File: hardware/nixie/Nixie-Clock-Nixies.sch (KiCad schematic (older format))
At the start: 21 parts, among them J1 Nixies-Connector

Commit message: Add screw terminals for I/O, Improve PCB layout
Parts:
- N1, N2, N3, N4, N5, N6: symbol nixies-us:IN-4 -> Nixie-Clock-Nixies-rescue:IN-4-nixies-us
- N10, N7, N8, N9: symbol nixies-us:IN-6 -> Nixie-Clock-Nixies-rescue:IN-6-nixies-us
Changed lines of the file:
@@
 $EndDescr
 $Comp
-L nixies-us:IN-4 N1
+L Nixie-Clock-Nixies-rescue:IN-4-nixies-us N1
 U 1 1 61C656EE
 P 1250 2800
@@
 $EndComp
 $Comp
-L nixies-us:IN-4 N2
+L Nixie-Clock-Nixies-rescue:IN-4-nixies-us N2
 U 1 1 61C66B88
 P 2850 2800
@@
 $EndComp
 $Comp
-L nixies-us:IN-6 N8
+L Nixie-Clock-Nixies-rescue:IN-6-nixies-us N8
 U 1 1 61C679B4
 P 3950 3100
@@
 $EndComp
 $Comp
-L nixies-us:IN-6 N7
+L Nixie-Clock-Nixies-rescue:IN-6-nixies-us N7
 U 1 1 61C6976E
 P 3950 2600
@@
 $EndComp
 $Comp
-L nixies-us:IN-4 N3
+L Nixie-Clock-Nixies-rescue:IN-4-nixies-us N3
 U 1 1 61C6CBC4
 P 5100 2800
@@
 $EndComp
 $Comp
-L nixies-us:IN-4 N4
+L Nixie-Clock-Nixies-rescue:IN-4-nixies-us N4
 U 1 1 61C6CBCA
 P 6700 2800
@@
 $EndComp
 $Comp
-L nixies-us:IN-6 N10
+L Nixie-Clock-Nixies-rescue:IN-6-nixies-us N10
 U 1 1 61C6CBD0
 P 7850 3100
@@
 $EndComp
 $Comp
-L nixies-us:IN-6 N9
+L Nixie-Clock-Nixies-rescue:IN-6-nixies-us N9
 U 1 1 61C6CBD6
 P 7850 2600
@@
 $EndComp
 $Comp
-L nixies-us:IN-4 N5
+L Nixie-Clock-Nixies-rescue:IN-4-nixies-us N5
 U 1 1 61C6E7AE
 P 9000 2800
@@
 $EndComp
 $Comp
-L nixies-us:IN-4 N6
+L Nixie-Clock-Nixies-rescue:IN-4-nixies-us N6
 U 1 1 61C6E7B4
 P 10600 2800

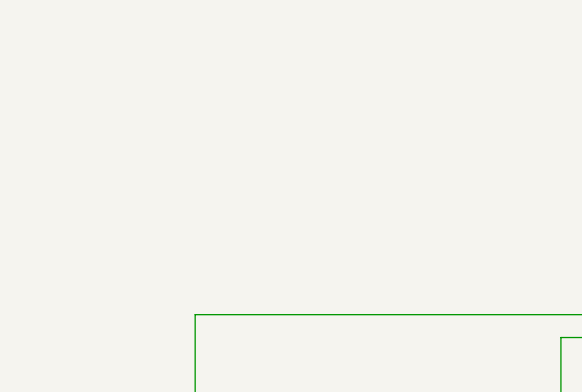
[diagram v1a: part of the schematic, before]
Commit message: Add Mounting Holes to PCB, Improve Routing, Add power pin header, Use correct connector footprint
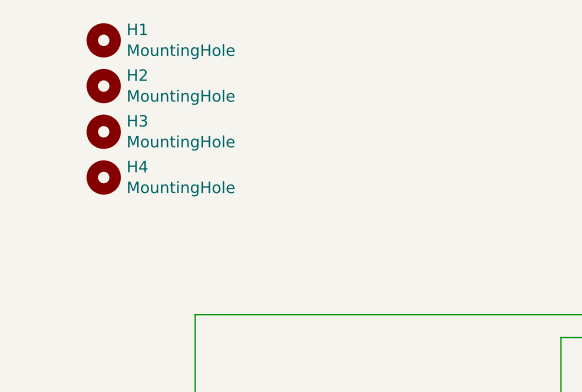
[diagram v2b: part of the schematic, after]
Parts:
- added H1, H2, H3, H4: MountingHole, MountingHole:MountingHole_2.7mm_M2.5, symbol Mechanical:MountingHole
- J1: footprint Connector_PinHeader_2.54mm:PinHeader_2x10_P2.54mm_Horizontal -> nixie-clock:PinHeader_2x10_P2.54mm_Horizontal_with_Interlock
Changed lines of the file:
@@
 F 0 "J1" V 5896 5612 50  0000 R CNN
 F 1 "Nixies-Connector" V 5805 5612 50  0000 R CNN
-F 2 "Connector_PinHeader_2.54mm:PinHeader_2x10_P2.54mm_Horizontal" H 5800 6200 50  0001 C CNN
+F 2 "nixie-clock:PinHeader_2x10_P2.54mm_Horizontal_with_Interlock" H 5800 6200 50  0001 C CNN
 F 3 "~" H 5800 6200 50  0001 C CNN
 	1    5800 6200
@@
 Wire Wire Line
 	3650 3450 3650 5100
+$Comp
+L Mechanical:MountingHole H2
+U 1 1 61CADA22
+P 850 1100
+F 0 "H2" H 950 1146 50  0000 L CNN
+F 1 "MountingHole" H 950 1055 50  0000 L CNN
+F 2 "MountingHole:MountingHole_2.7mm_M2.5" H 850 1100 50  0001 C CNN
+F 3 "~" H 850 1100 50  0001 C CNN
+	1    850  1100
+	1    0    0    -1
+$EndComp
+$Comp
+L Mechanical:MountingHole H3
+U 1 1 61CAE12D
+P 850 1300
+F 0 "H3" H 950 1346 50  0000 L CNN
+F 1 "MountingHole" H 950 1255 50  0000 L CNN
+F 2 "MountingHole:MountingHole_2.7mm_M2.5" H 850 1300 50  0001 C CNN
+F 3 "~" H 850 1300 50  0001 C CNN
+	1    850  1300
+	1    0    0    -1
+$EndComp
+$Comp
+L Mechanical:MountingHole H4
+U 1 1 61CAE6FB
+P 850 1500
+F 0 "H4" H 950 1546 50  0000 L CNN
+F 1 "MountingHole" H 950 1455 50  0000 L CNN
+F 2 "MountingHole:MountingHole_2.7mm_M2.5" H 850 1500 50  0001 C CNN
+F 3 "~" H 850 1500 50  0001 C CNN
+	1    850  1500
+	1    0    0    -1
+$EndComp
+$Comp
+L Mechanical:MountingHole H1
+U 1 1 61CACF00
+P 850 900
+F 0 "H1" H 950 946 50  0000 L CNN
+F 1 "MountingHole" H 950 855 50  0000 L CNN
+F 2 "MountingHole:MountingHole_2.7mm_M2.5" H 850 900 50  0001 C CNN
+F 3 "~" H 850 900 50  0001 C CNN
+	1    850  900
+	1    0    0    -1
+$EndComp
 $EndSCHEMATC

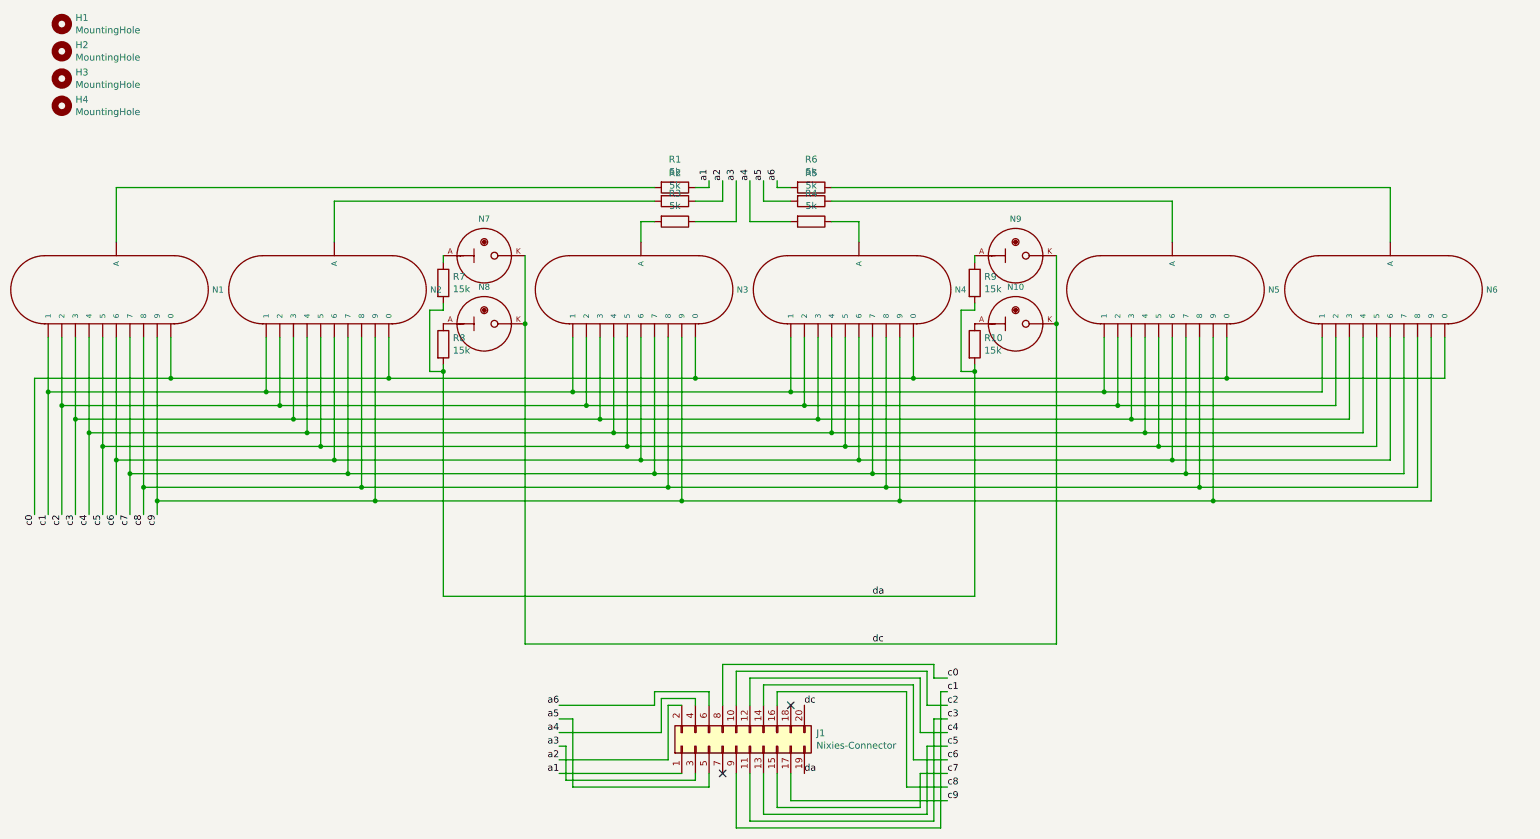
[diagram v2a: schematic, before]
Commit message: Fix libraries used in Nixie-Clock-Nixies
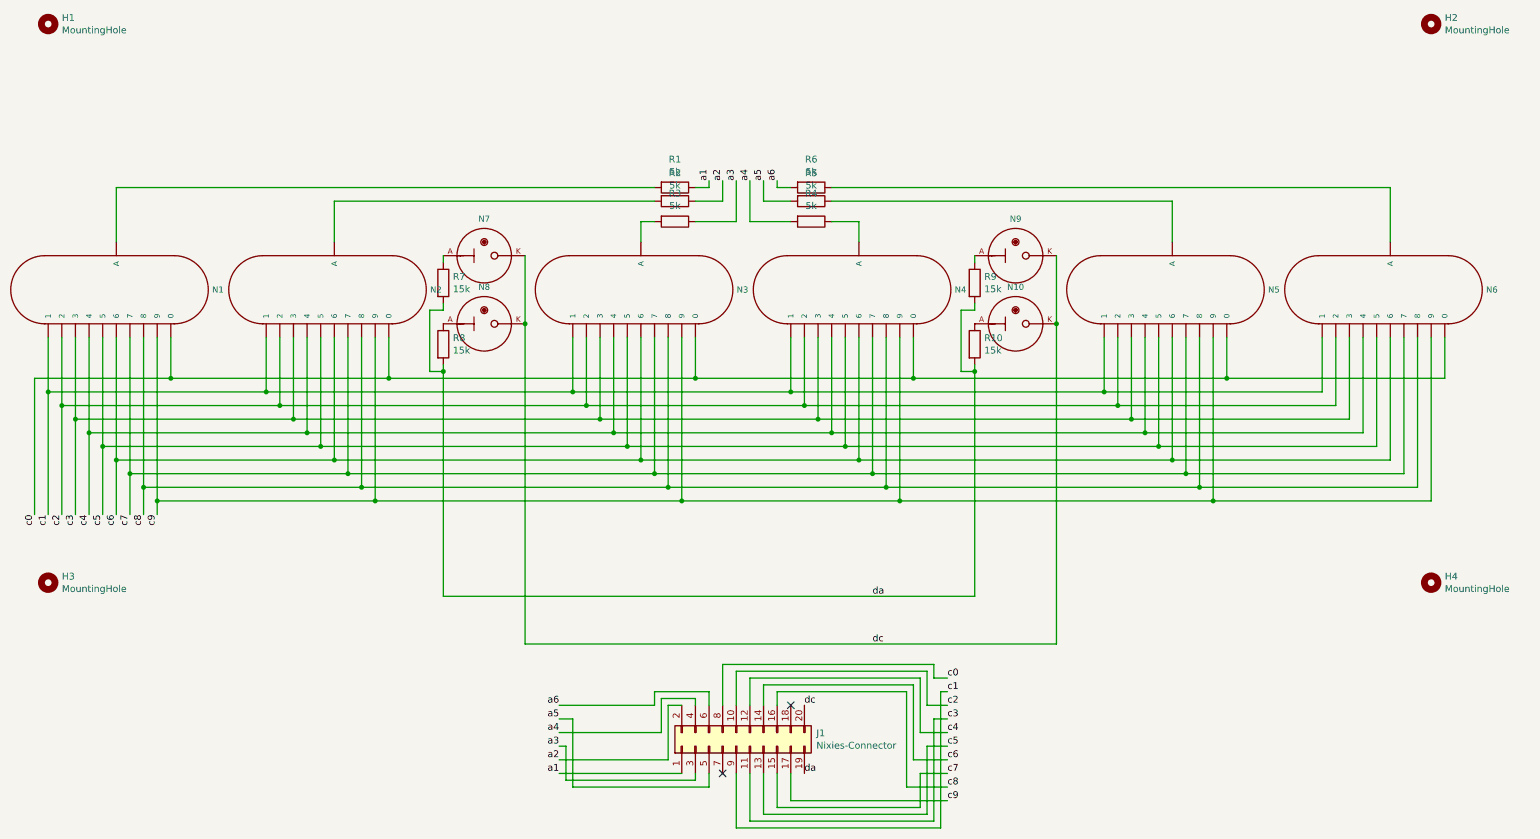
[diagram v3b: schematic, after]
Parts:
- removed N1, N2, N3, N4, N5, N6: IN-4, nixies-us:nixies-us-IN-4-DSUB, symbol Nixie-Clock-Nixies-rescue:IN-4-nixies-us
- removed N10, N7, N8, N9: IN-6, nixies-us:nixies-us-IN-6, symbol Nixie-Clock-Nixies-rescue:IN-6-nixies-us
- added N1, N2, N3, N4, N5, N6: IN-4, nixies-us:nixies-us-IN-4-DSUB, symbol nixies-us:IN-4
- added N10, N7, N8, N9: IN-6, nixies-us:nixies-us-IN-6, symbol nixies-us:IN-6
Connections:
- net c0: now also N1.0, N2.0, N3.0, N4.0, N5.0, N6.0
- net c1: now also N1.1, N2.1, N3.1, N4.1, N5.1, N6.1
- net c2: now also N1.2, N2.2, N3.2, N4.2, N5.2, N6.2
- net c3: now also N1.3, N2.3, N3.3, N4.3, N5.3, N6.3
- net c4: now also N1.4, N2.4, N3.4, N4.4, N5.4, N6.4
- net c5: now also N1.5, N2.5, N3.5, N4.5, N5.5, N6.5
- net c6: now also N1.6, N2.6, N3.6, N4.6, N5.6, N6.6
- net c7: now also N1.7, N2.7, N3.7, N4.7, N5.7, N6.7
- net c8: now also N1.8, N2.8, N3.8, N4.8, N5.8, N6.8
- net c9: now also N1.9, N2.9, N3.9, N4.9, N5.9, N6.9
- net dc: now also N10.K, N7.K, N8.K, N9.K
- net at R3.2: now also N3.A3 (A)
- net at R2.2: now also N2.A3 (A)
- net at R1.2: now also N1.A3 (A)
- net at R6.1: now also N6.A3 (A)
- net at R5.1: now also N5.A3 (A)
- net at R4.1: now also N4.A3 (A)
- net at R8.1: now also N8.A
- net at R7.1: now also N7.A
- net at R10.1: now also N10.A
- net at R9.1: now also N9.A
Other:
- moved on the sheet: H1, H2, H3, H4
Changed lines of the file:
@@
 encoding utf-8
 Sheet 1 1
-Title ""
-Date ""
-Rev ""
-Comp ""
+Title "Nixie-Clock: Nixies"
+Date "2021-12-25"
+Rev "1.0"
+Comp "Konrad Mösch"
 Comment1 ""
 Comment2 ""
@@
 Comment4 ""
 $EndDescr
-$Comp
-L Nixie-Clock-Nixies-rescue:IN-4-nixies-us N1
-U 1 1 61C656EE
-P 1250 2800
-F 0 "N1" V 1200 2097 45  0000 R CNN
-F 1 "IN-4" H 1250 2800 45  0001 L BNN
-F 2 "nixies-us:nixies-us-IN-4-DSUB" H 1280 2950 20  0001 C CNN
-F 3 "" H 1250 2800 50  0001 C CNN
-	1    1250 2800
-	0    -1   -1   0
-$EndComp
-$Comp
-L Nixie-Clock-Nixies-rescue:IN-4-nixies-us N2
-U 1 1 61C66B88
-P 2850 2800
-F 0 "N2" V 2800 2097 45  0000 R CNN
-F 1 "IN-4" H 2850 2800 45  0001 L BNN
-F 2 "nixies-us:nixies-us-IN-4-DSUB" H 2880 2950 20  0001 C CNN
-F 3 "" H 2850 2800 50  0001 C CNN
-	1    2850 2800
-	0    -1   -1   0
-$EndComp
-$Comp
-L Nixie-Clock-Nixies-rescue:IN-6-nixies-us N8
-U 1 1 61C679B4
-P 3950 3100
-F 0 "N8" H 3950 3370 45  0000 C CNN
-F 1 "IN-6" H 3950 3100 45  0001 L BNN
-F 2 "nixies-us:nixies-us-IN-6" H 3980 3250 20  0001 C CNN
-F 3 "" H 3950 3100 50  0001 C CNN
-	1    3950 3100
-	1    0    0    -1
-$EndComp
-$Comp
-L Nixie-Clock-Nixies-rescue:IN-6-nixies-us N7
-U 1 1 61C6976E
-P 3950 2600
-F 0 "N7" H 3950 2870 45  0000 C CNN
-F 1 "IN-6" H 3950 2600 45  0001 L BNN
-F 2 "nixies-us:nixies-us-IN-6" H 3980 2750 20  0001 C CNN
-F 3 "" H 3950 2600 50  0001 C CNN
-	1    3950 2600
-	1    0    0    -1
-$EndComp
-$Comp
-L Nixie-Clock-Nixies-rescue:IN-4-nixies-us N3
-U 1 1 61C6CBC4
-P 5100 2800
-F 0 "N3" V 5050 2097 45  0000 R CNN
-F 1 "IN-4" H 5100 2800 45  0001 L BNN
-F 2 "nixies-us:nixies-us-IN-4-DSUB" H 5130 2950 20  0001 C CNN
-F 3 "" H 5100 2800 50  0001 C CNN
-	1    5100 2800
-	0    -1   -1   0
-$EndComp
-$Comp
-L Nixie-Clock-Nixies-rescue:IN-4-nixies-us N4
-U 1 1 61C6CBCA
-P 6700 2800
-F 0 "N4" V 6650 2097 45  0000 R CNN
-F 1 "IN-4" H 6700 2800 45  0001 L BNN
-F 2 "nixies-us:nixies-us-IN-4-DSUB" H 6730 2950 20  0001 C CNN
-F 3 "" H 6700 2800 50  0001 C CNN
-	1    6700 2800
-	0    -1   -1   0
-$EndComp
-$Comp
-L Nixie-Clock-Nixies-rescue:IN-6-nixies-us N10
-U 1 1 61C6CBD0
-P 7850 3100
-F 0 "N10" H 7850 3370 45  0000 C CNN
-F 1 "IN-6" H 7850 3100 45  0001 L BNN
-F 2 "nixies-us:nixies-us-IN-6" H 7880 3250 20  0001 C CNN
-F 3 "" H 7850 3100 50  0001 C CNN
-	1    7850 3100
-	1    0    0    -1
-$EndComp
-$Comp
-L Nixie-Clock-Nixies-rescue:IN-6-nixies-us N9
-U 1 1 61C6CBD6
-P 7850 2600
-F 0 "N9" H 7850 2870 45  0000 C CNN
-F 1 "IN-6" H 7850 2600 45  0001 L BNN
-F 2 "nixies-us:nixies-us-IN-6" H 7880 2750 20  0001 C CNN
-F 3 "" H 7850 2600 50  0001 C CNN
-	1    7850 2600
-	1    0    0    -1
-$EndComp
-$Comp
-L Nixie-Clock-Nixies-rescue:IN-4-nixies-us N5
-U 1 1 61C6E7AE
-P 9000 2800
-F 0 "N5" V 8950 2097 45  0000 R CNN
-F 1 "IN-4" H 9000 2800 45  0001 L BNN
-F 2 "nixies-us:nixies-us-IN-4-DSUB" H 9030 2950 20  0001 C CNN
-F 3 "" H 9000 2800 50  0001 C CNN
-	1    9000 2800
-	0    -1   -1   0
-$EndComp
-$Comp
-L Nixie-Clock-Nixies-rescue:IN-4-nixies-us N6
-U 1 1 61C6E7B4
-P 10600 2800
-F 0 "N6" V 10550 2097 45  0000 R CNN
-F 1 "IN-4" H 10600 2800 45  0001 L BNN
-F 2 "nixies-us:nixies-us-IN-4-DSUB" H 10630 2950 20  0001 C CNN
-F 3 "" H 10600 2800 50  0001 C CNN
-	1    10600 2800
-	0    -1   -1   0
-$EndComp
 Wire Wire Line
 	3650 2600 3650 2650
 Wire Wire Line
 	7550 2600 7550 2650
-Wire Wire Line
-	4250 2600 4250 3100
-Wire Wire Line
-	8150 2600 8150 3100
 Wire Wire Line
 	5800 2350 5500 2350
@@
 Wire Wire Line
 	7100 3500 9400 3500
-Connection ~ 4250 3100
-Connection ~ 8150 3100
-Wire Wire Line
-	8150 3100 8150 5450
-Wire Wire Line
-	4250 3100 4250 5450
 Wire Wire Line
 	11000 3200 11000 3500
@@
 L Mechanical:MountingHole H2
 U 1 1 61CADA22
-P 850 1100
-F 0 "H2" H 950 1146 50  0000 L CNN
-F 1 "MountingHole" H 950 1055 50  0000 L CNN
-F 2 "MountingHole:MountingHole_2.7mm_M2.5" H 850 1100 50  0001 C CNN
-F 3 "~" H 850 1100 50  0001 C CNN
-	1    850  1100
+P 10900 900
+F 0 "H2" H 11000 946 50  0000 L CNN
+F 1 "MountingHole" H 11000 855 50  0000 L CNN
+F 2 "MountingHole:MountingHole_2.7mm_M2.5" H 10900 900 50  0001 C CNN
+F 3 "~" H 10900 900 50  0001 C CNN
+	1    10900 900
 	1    0    0    -1
 $EndComp
@@
 L Mechanical:MountingHole H3
 U 1 1 61CAE12D
-P 850 1300
-F 0 "H3" H 950 1346 50  0000 L CNN
-F 1 "MountingHole" H 950 1255 50  0000 L CNN
-F 2 "MountingHole:MountingHole_2.7mm_M2.5" H 850 1300 50  0001 C CNN
-F 3 "~" H 850 1300 50  0001 C CNN
-	1    850  1300
+P 750 5000
+F 0 "H3" H 850 5046 50  0000 L CNN
+F 1 "MountingHole" H 850 4955 50  0000 L CNN
+F 2 "MountingHole:MountingHole_2.7mm_M2.5" H 750 5000 50  0001 C CNN
+F 3 "~" H 750 5000 50  0001 C CNN
+	1    750  5000
 	1    0    0    -1
 $EndComp
@@
 L Mechanical:MountingHole H4
 U 1 1 61CAE6FB
-P 850 1500
-F 0 "H4" H 950 1546 50  0000 L CNN
-F 1 "MountingHole" H 950 1455 50  0000 L CNN
-F 2 "MountingHole:MountingHole_2.7mm_M2.5" H 850 1500 50  0001 C CNN
-F 3 "~" H 850 1500 50  0001 C CNN
-	1    850  1500
+P 10900 5000
+F 0 "H4" H 11000 5046 50  0000 L CNN
+F 1 "MountingHole" H 11000 4955 50  0000 L CNN
+F 2 "MountingHole:MountingHole_2.7mm_M2.5" H 10900 5000 50  0001 C CNN
+F 3 "~" H 10900 5000 50  0001 C CNN
+	1    10900 5000
 	1    0    0    -1
 $EndComp
@@
 L Mechanical:MountingHole H1
 U 1 1 61CACF00
-P 850 900
-F 0 "H1" H 950 946 50  0000 L CNN
-F 1 "MountingHole" H 950 855 50  0000 L CNN
-F 2 "MountingHole:MountingHole_2.7mm_M2.5" H 850 900 50  0001 C CNN
-F 3 "~" H 850 900 50  0001 C CNN
-	1    850  900
-	1    0    0    -1
-$EndComp
+P 750 900
+F 0 "H1" H 850 946 50  0000 L CNN
+F 1 "MountingHole" H 850 855 50  0000 L CNN
+F 2 "MountingHole:MountingHole_2.7mm_M2.5" H 750 900 50  0001 C CNN
+F 3 "~" H 750 900 50  0001 C CNN
+	1    750  900
+	1    0    0    -1
+$EndComp
+Wire Wire Line
+	4250 2600 4250 3100
+Wire Wire Line
+	8150 2600 8150 3100
+$Comp
+L nixies-us:IN-4 N1
+U 1 1 61C87710
+P 1250 2800
+F 0 "N1" V 1200 2097 45  0000 R CNN
+F 1 "IN-4" H 1250 2800 45  0001 L BNN
+F 2 "nixies-us:nixies-us-IN-4-DSUB" H 1280 2950 20  0001 C CNN
+F 3 "" H 1250 2800 50  0001 C CNN
+	1    1250 2800
+	0    -1   -1   0
+$EndComp
+$Comp
+L nixies-us:IN-4 N2
+U 1 1 61CA8401
+P 2850 2800
+F 0 "N2" V 2800 2097 45  0000 R CNN
+F 1 "IN-4" H 2850 2800 45  0001 L BNN
+F 2 "nixies-us:nixies-us-IN-4-DSUB" H 2880 2950 20  0001 C CNN
+F 3 "" H 2850 2800 50  0001 C CNN
+	1    2850 2800
+	0    -1   -1   0
+$EndComp
+$Comp
+L nixies-us:IN-4 N3
+U 1 1 61CAC5E2
+P 5100 2800
+F 0 "N3" V 5050 2097 45  0000 R CNN
+F 1 "IN-4" H 5100 2800 45  0001 L BNN
+F 2 "nixies-us:nixies-us-IN-4-DSUB" H 5130 2950 20  0001 C CNN
+F 3 "" H 5100 2800 50  0001 C CNN
+	1    5100 2800
+	0    -1   -1   0
+$EndComp
+$Comp
+L nixies-us:IN-4 N4
+U 1 1 61CAC7D4
+P 6700 2800
+F 0 "N4" V 6650 2097 45  0000 R CNN
+F 1 "IN-4" H 6700 2800 45  0001 L BNN
+F 2 "nixies-us:nixies-us-IN-4-DSUB" H 6730 2950 20  0001 C CNN
+F 3 "" H 6700 2800 50  0001 C CNN
+	1    6700 2800
+	0    -1   -1   0
+$EndComp
+$Comp
+L nixies-us:IN-4 N5
+U 1 1 61D07B84
+P 9000 2800
+F 0 "N5" V 8950 2097 45  0000 R CNN
+F 1 "IN-4" H 9000 2800 45  0001 L BNN
+F 2 "nixies-us:nixies-us-IN-4-DSUB" H 9030 2950 20  0001 C CNN
+F 3 "" H 9000 2800 50  0001 C CNN
+	1    9000 2800
+	0    -1   -1   0
+$EndComp
+$Comp
+L nixies-us:IN-4 N6
+U 1 1 61D07B8A
+P 10600 2800
+F 0 "N6" V 10550 2097 45  0000 R CNN
+F 1 "IN-4" H 10600 2800 45  0001 L BNN
+F 2 "nixies-us:nixies-us-IN-4-DSUB" H 10630 2950 20  0001 C CNN
+F 3 "" H 10600 2800 50  0001 C CNN
+	1    10600 2800
+	0    -1   -1   0
+$EndComp
+$Comp
+L nixies-us:IN-6 N7
+U 1 1 61D34690
+P 3950 2600
+F 0 "N7" H 3950 2870 45  0000 C CNN
+F 1 "IN-6" H 3950 2600 45  0001 L BNN
+F 2 "nixies-us:nixies-us-IN-6" H 3980 2750 20  0001 C CNN
+F 3 "" H 3950 2600 50  0001 C CNN
+	1    3950 2600
+	1    0    0    -1
+$EndComp
+$Comp
+L nixies-us:IN-6 N8
+U 1 1 61D37441
+P 3950 3100
+F 0 "N8" H 3950 3370 45  0000 C CNN
+F 1 "IN-6" H 3950 3100 45  0001 L BNN
+F 2 "nixies-us:nixies-us-IN-6" H 3980 3250 20  0001 C CNN
+F 3 "" H 3950 3100 50  0001 C CNN
+	1    3950 3100
+	1    0    0    -1
+$EndComp
+Connection ~ 4250 3100
+Wire Wire Line
+	4250 3100 4250 5450
+$Comp
+L nixies-us:IN-6 N9
+U 1 1 61D38F4A
+P 7850 2600
+F 0 "N9" H 7850 2870 45  0000 C CNN
+F 1 "IN-6" H 7850 2600 45  0001 L BNN
+F 2 "nixies-us:nixies-us-IN-6" H 7880 2750 20  0001 C CNN
+F 3 "" H 7850 2600 50  0001 C CNN
+	1    7850 2600
+	1    0    0    -1
+$EndComp
+$Comp
+L nixies-us:IN-6 N10
+U 1 1 61D38F50
+P 7850 3100
+F 0 "N10" H 7850 3370 45  0000 C CNN
+F 1 "IN-6" H 7850 3100 45  0001 L BNN
+F 2 "nixies-us:nixies-us-IN-6" H 7880 3250 20  0001 C CNN
+F 3 "" H 7850 3100 50  0001 C CNN
+	1    7850 3100
+	1    0    0    -1
+$EndComp
+Connection ~ 8150 3100
+Wire Wire Line
+	8150 3100 8150 5450
 $EndSCHEMATC
